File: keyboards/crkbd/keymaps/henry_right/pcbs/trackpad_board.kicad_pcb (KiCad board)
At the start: 2 copper layers, 48.4 x 19.9 mm, 6 parts, among them J1 67997-410HLF, J2 DF30FB-20DS-0.4V(82)

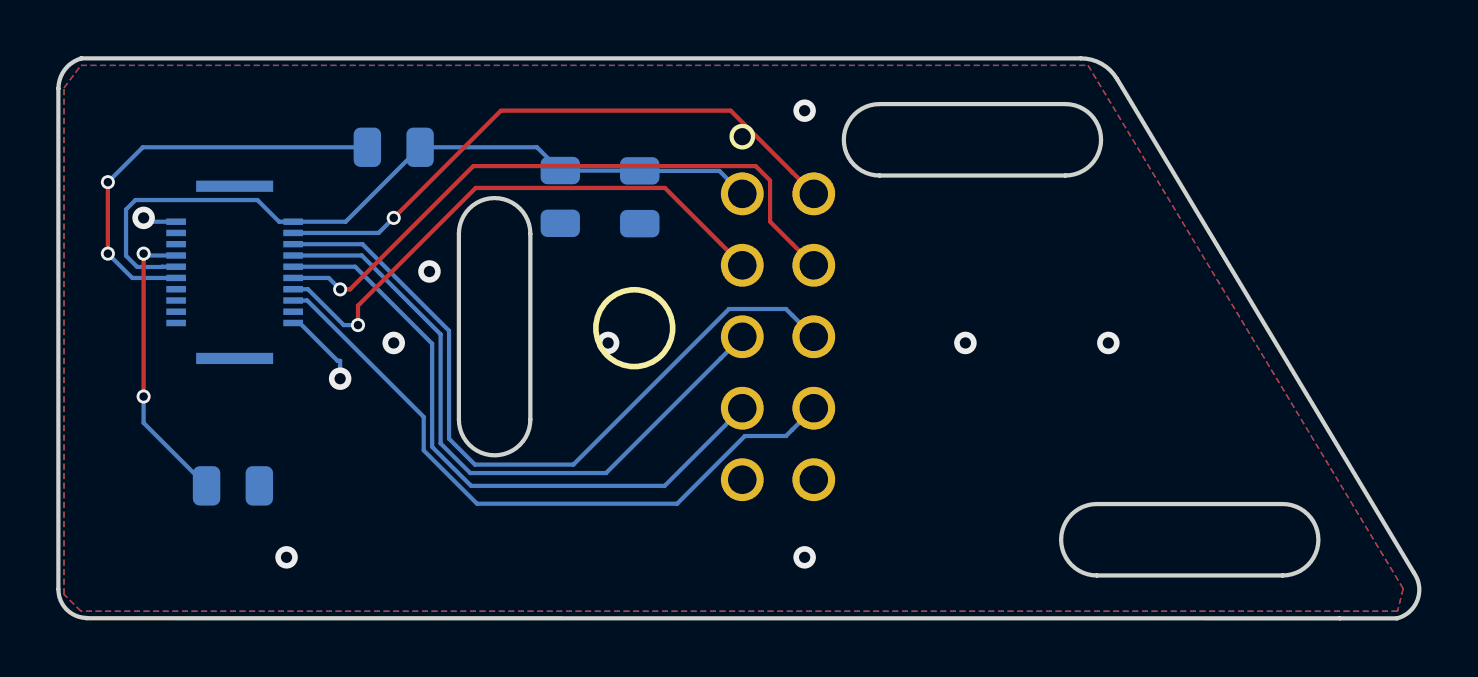
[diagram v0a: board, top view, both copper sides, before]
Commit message: 좀 더 위쪽으로 옮기고, 이름 새기기
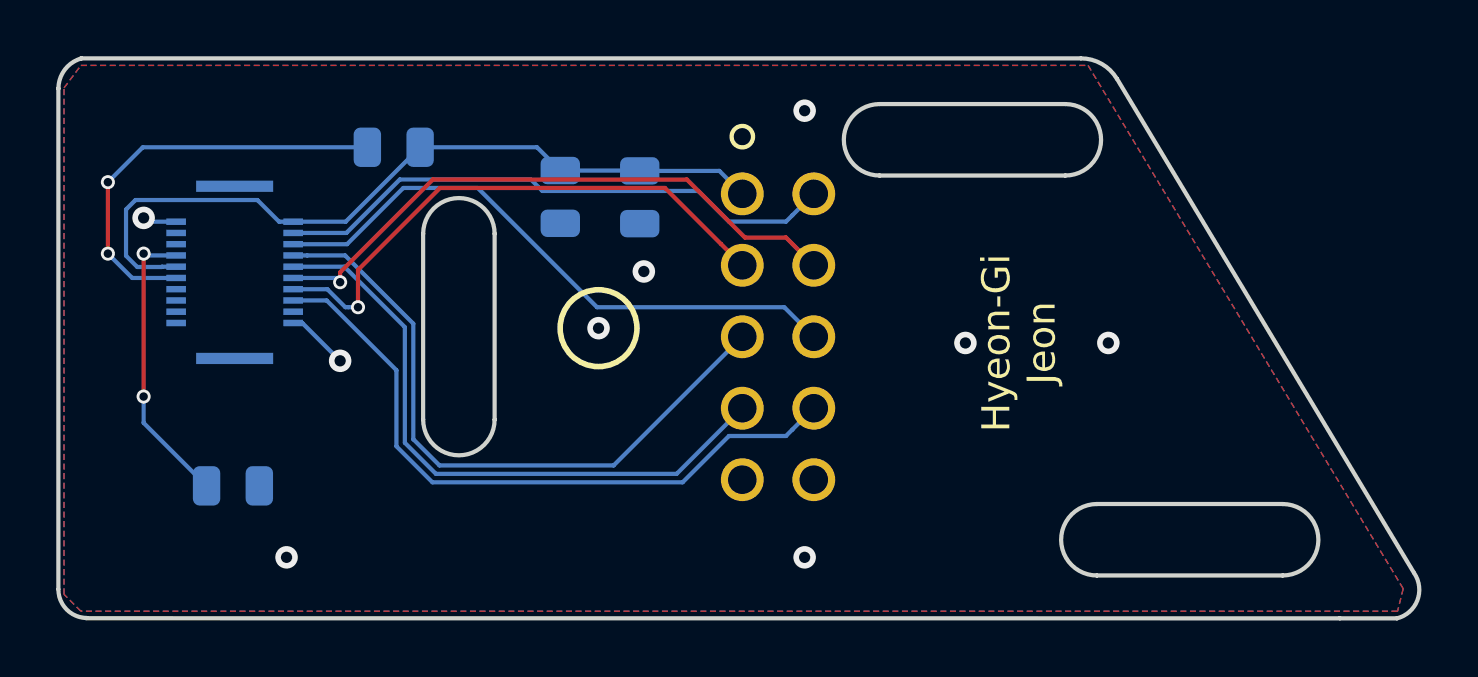
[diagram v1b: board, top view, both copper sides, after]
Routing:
- net MISO_2V85: track 26.7 -> 21.5 mm
- net TP_CS_2V85: track 22.8 -> 21.5 mm
- net TP_MOTION_2V85: track 21.5 -> 20.3 mm, vias 1 -> 0
- net GND: track 4.07 -> 3.44 mm, vias 10 -> 9
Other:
- outline, holes or cut-outs redrawn
- board text added: "Hyeon-Gi Jeon"
